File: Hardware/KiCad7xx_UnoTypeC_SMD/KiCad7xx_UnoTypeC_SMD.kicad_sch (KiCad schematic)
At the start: 75 parts, among them J1 -, J1 USB_C_Receptacle_USB2.0, J2 PINHD-1X18, T1 FDN340P, U1 MC33269ST, U2 LP2985-XXDBVR, U3 ATMEGA16U2, U4 ATmega328PB-A, U5 LMV358?MM, X1 POWERSUPPLY_DC21MMX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

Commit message: feat: 変更した部品のフットプリントを再度配線
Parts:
- removed TP_USH0: TP_SP, UNOSMD_V3:TP-SP, symbol UNOSMD_V3-eagle-import:TP_SP
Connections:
- net +5V: now also U4.4 (VCC)
- net GND: no longer U4.4 (VCC)
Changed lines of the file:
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@@
   (junction (at 270.51 177.8) (diameter 0) (color 0 0 0 0)
   )
-  (junction (at 71.12 185.42) (diameter 0) (color 0 0 0 0)
-  )
   (junction (at 144.78 147.32) (diameter 0) (color 0 0 0 0)
   )
@@
   (junction (at 154.94 68.58) (diameter 0) (color 0 0 0 0)
   )
+  (junction (at 304.8 182.88) (diameter 0) (color 0 0 0 0)
+  )
   (junction (at 261.62 198.12) (diameter 0) (color 0 0 0 0)
   )
@@
   )
   (junction (at 284.48 128.27) (diameter 0) (color 0 0 0 0)
-  )
-  (junction (at 304.8 190.5) (diameter 0) (color 0 0 0 0)
   )
   (junction (at 334.01 196.85) (diameter 0) (color 0 0 0 0)
@@
     (stroke (width 0.1524) (type solid))
   )
-  (wire (pts (xy 44.45 185.42) (xy 71.12 185.42))
-    (stroke (width 0.1524) (type solid))
-  )
   (wire (pts (xy 101.6 127) (xy 121.92 127))
     (stroke (width 0.1524) (type solid))
@@
     (stroke (width 0.1524) (type solid))
   )
-  (wire (pts (xy 71.12 185.42) (xy 80.01 185.42))
+  (wire (pts (xy 44.45 185.42) (xy 80.01 185.42))
     (stroke (width 0.1524) (type solid))
   )
@@
     (stroke (width 0.1524) (type solid))
   )
+  (wire (pts (xy 309.88 190.5) (xy 309.88 182.88))
+    (stroke (width 0.1524) (type solid))
+  )
   (wire (pts (xy 309.88 110.49) (xy 287.02 110.49))
     (stroke (width 0.1524) (type solid))
@@
     (stroke (width 0) (type default))
   )
-  (wire (pts (xy 304.8 190.5) (xy 325.12 190.5))
+  (wire (pts (xy 309.88 190.5) (xy 325.12 190.5))
     (stroke (width 0.1524) (type solid))
   )
@@
     (stroke (width 0.1524) (type solid))
   )
-  (wire (pts (xy 71.12 180.34) (xy 71.12 185.42))
-    (stroke (width 0.1524) (type solid))
-  )
   (wire (pts (xy 67.31 162.56) (xy 67.31 165.1))
     (stroke (width 0) (type default))
@@
   )
   (wire (pts (xy 111.76 200.66) (xy 111.76 187.96))
+    (stroke (width 0.1524) (type solid))
+  )
+  (wire (pts (xy 309.88 182.88) (xy 304.8 182.88))
     (stroke (width 0.1524) (type solid))
   )
@@
         )
       )
-    )
-  )
-  (symbol (lib_id "UNOSMD_V3-eagle-import:TP_SP") (at 71.12 180.34 90) (unit 1)
-    (in_bom yes) (on_board yes) (dnp no)
-    (property "Reference" "TP_USH0" (at 68.58 175.26 90)
-      (effects (font (size 1.27 1.0795)) (justify right top) hide)
-    )
-    (property "Value" "TP_SP" (at 71.12 180.34 0)
-      (effects (font (size 1.27 1.27)) hide)
-    )
-    (property "Footprint" "UNOSMD_V3:TP-SP" (at 71.12 180.34 0)
-      (effects (font (size 1.27 1.27)) hide)
-    )
-    (property "Datasheet" "" (at 71.12 180.34 0)
-      (effects (font (size 1.27 1.27)) hide)
-    )
-    (pin "X")
-    (instances
-      (project "KiCad7xx_UnoTypeC_SMD"
-        (path "/a7599d81-3c40-47b2-86ef-613d133f34b5"
-          (reference "TP_USH0") (unit 1)
-        )
-      )

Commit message: feat: 電源回路を見直しダイオードSS54B(FOSAN)の追加
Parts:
- removed D1: M7, UNOSMD_V3:SMB, symbol UNOSMD_V3-eagle-import:DIODE-SMB
- removed U5: LMV358?MM, UNOSMD_V3:MSOP08, symbol UNOSMD_V3-eagle-import:LMV358?MM
- added D1, D4: SS54B (FOSAN), Diode_SMD:D_SMB, symbol Device:D_Schottky_Small
- added U5: LMV358IDGKR, UNOSMD_V3:MSOP08, symbol Texas_OPAmpDual_LMV358IDGKR_SnapEDA:LMV358IDGKR
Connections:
- net +3V3: now also U5.2
- net +5V: now also U5.8 (VCC+)
- net CMP: now also U5.3
- net GATE_CMD: now also U5.1
- net GND: now also U5.4 (GND)
- net L13: now also U5.6, U5.7
- net PWRIN: now also D1.2 (A)
- net SCK: now also U5.5
- net VIN: now also D4.2 (A); no longer PC1.+, RN1.8 (2), U1.3 (IN)
- new net VCC: D1.1 (K), D4.1 (K), PC1.+, RN1.8 (2), U1.3 (IN)
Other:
- moved on the sheet: C1

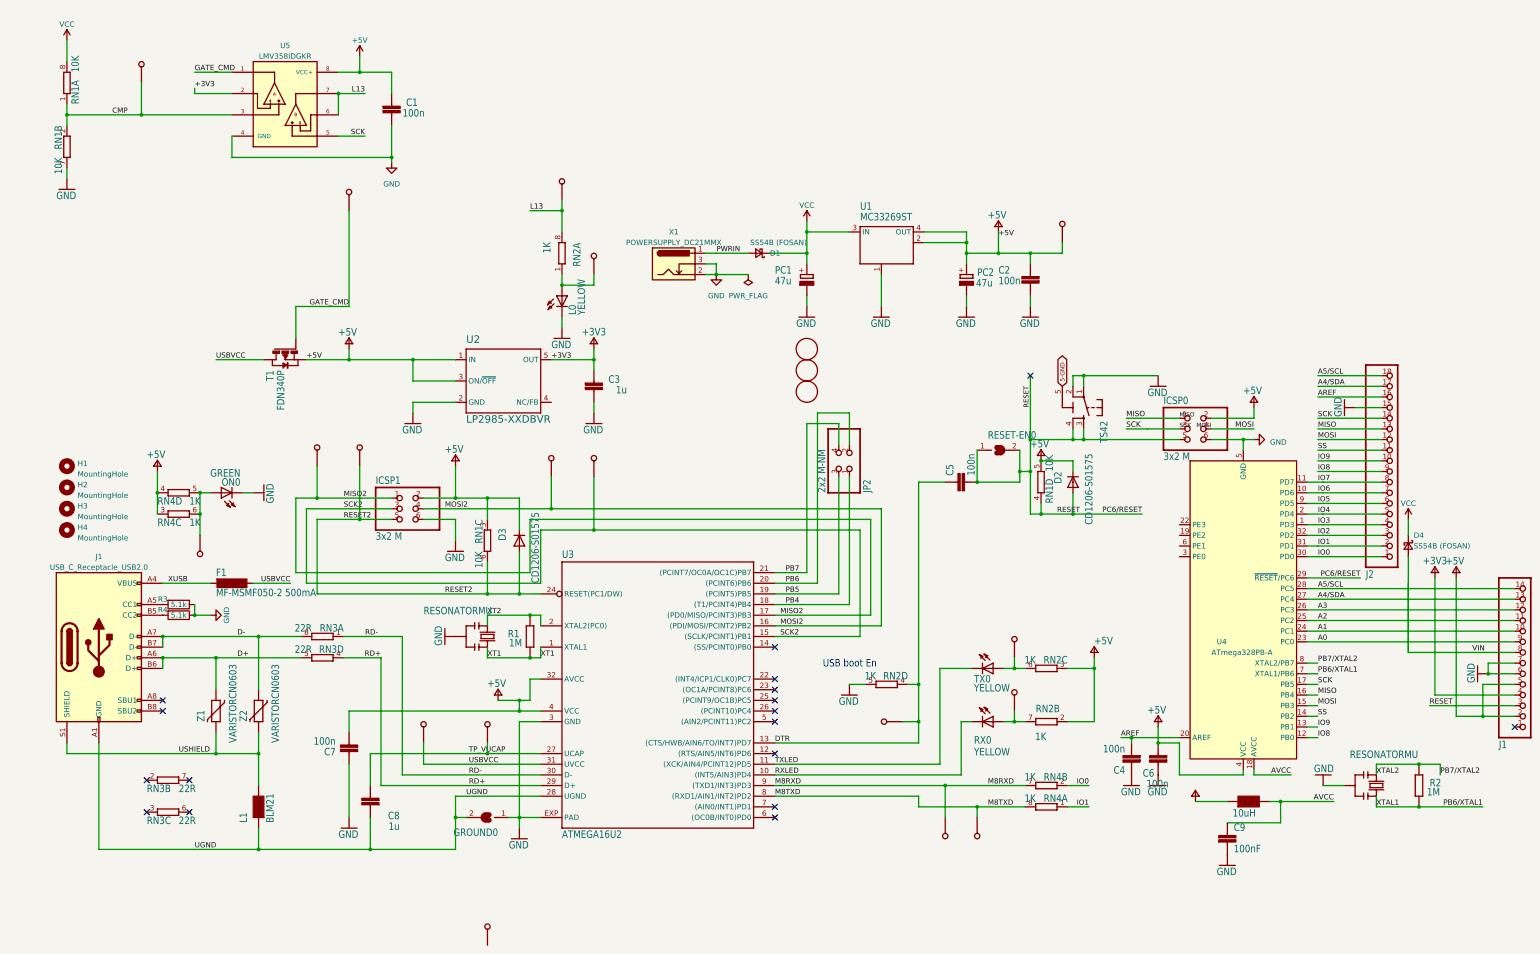
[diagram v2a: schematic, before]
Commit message: feat: UnoTypeC_SMD Rev1Cのガーバファイルを作成
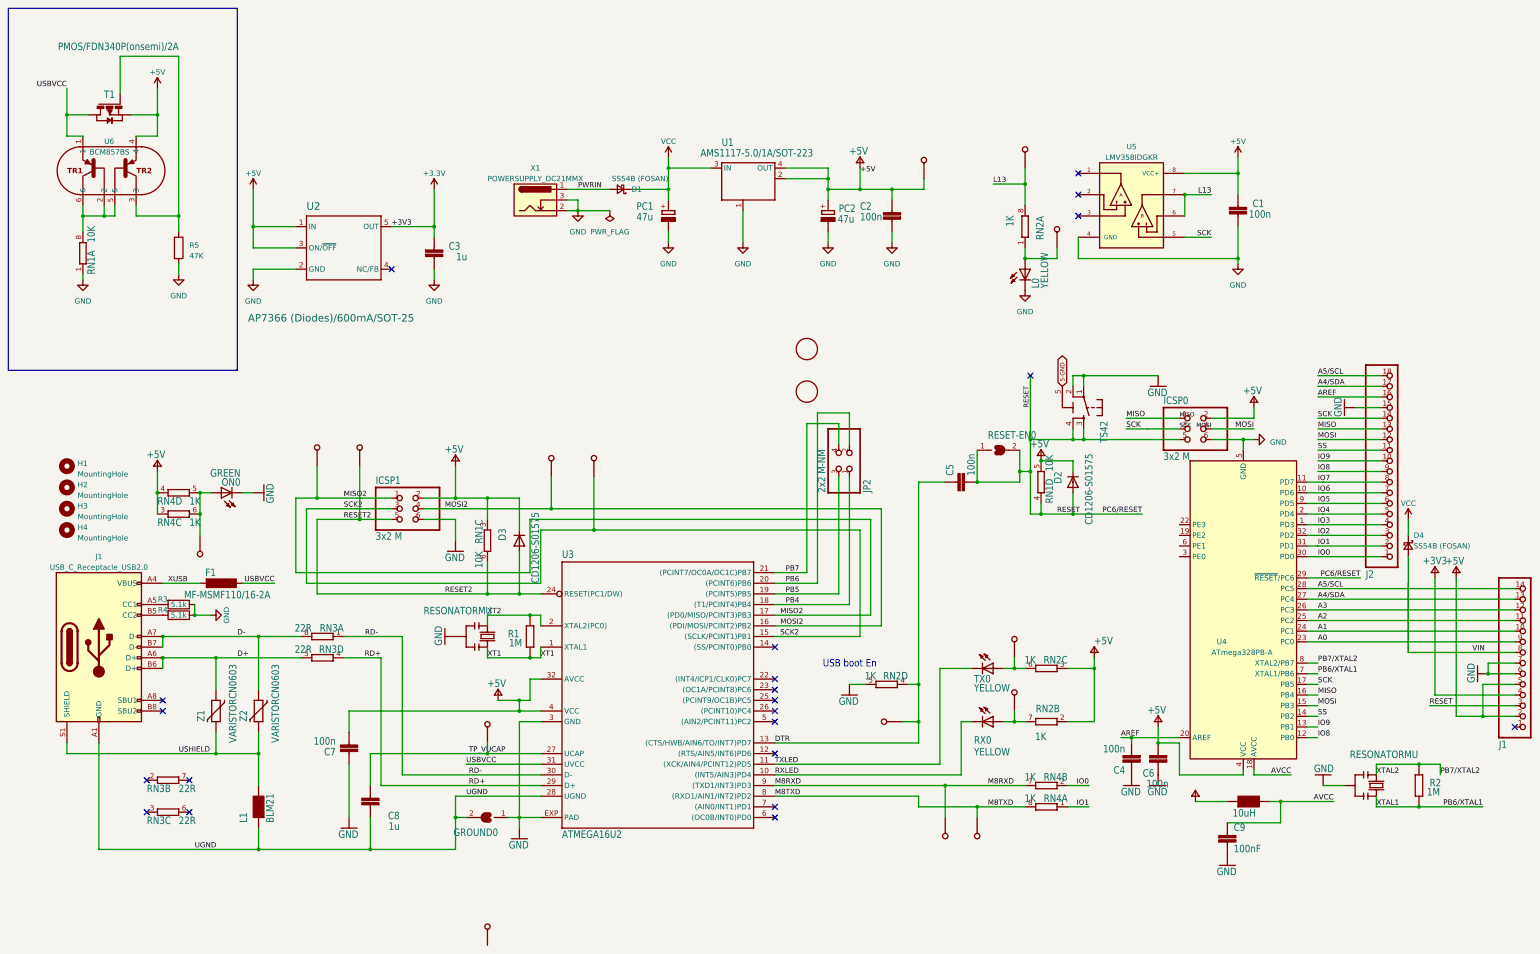
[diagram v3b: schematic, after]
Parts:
- removed FD2: FIDUCIAL-1.5MM, UNOSMD_V3:FD-1-1.5, symbol UNOSMD_V3-eagle-import:FIDUCIAL-1.5MM
- removed unit 2 of RN1
- removed TP_CMP0, TP_GATE0, TP_USBVCC0: TP_SP, UNOSMD_V3:TP-SP, symbol UNOSMD_V3-eagle-import:TP_SP
- added R5: 47K, Resistor_SMD:R_0603_1608Metric, symbol Device:R
- added U6: BCM857BS, Nexperia_TRANSISTOR_BCM857BS_SOT-363_Component:SOT65P210X110-6N, symbol Nexperia_TRANSISTOR_BCM857BS_SOT-363_Component:BCM857BS__1
- F1: value MF-MSMF050-2 500mA -> MF-MSMF110/16-2A
- T1: value FDN340P -> PMOS/FDN340P(onsemi)/2A
- U1: value MC33269ST -> AMS1117-5.0/1A/SOT-223
- U2: value LP2985-XXDBVR -> AP7366 (Diodes)/600mA/SOT-25
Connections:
- net +5V: now also U6.4
- net GND: now also RN1.1, R5.2
- net USBVCC: now also U6.1
- net VCC: no longer RN1.8 (2)
- net +3V3 renamed +3.3V
- net +3.3V: no longer U5.2
- net CMP: no longer names the net of U5.3
- net CMP: no longer RN1.1
- net GATE_CMD: no longer names the net of T1.3 (G)
- net GATE_CMD: now also R5.1, U6.3; no longer U5.1
- new net: RN1.8 (2), U6.2, U6.5, U6.6
- no-connect marks 17 -> 21
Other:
- moved on the sheet: C1, C2, C3, D1, F1, L0, PC1, PC2, RN2A, U1, U2, U5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
